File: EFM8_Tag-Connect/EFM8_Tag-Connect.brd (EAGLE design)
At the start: 10 parts, among them J1 MF-CON-2.54mm-01x08, J2 MF-CON-2.54mm-01x07, U1 EFM8BB10F2G-A-QFN20

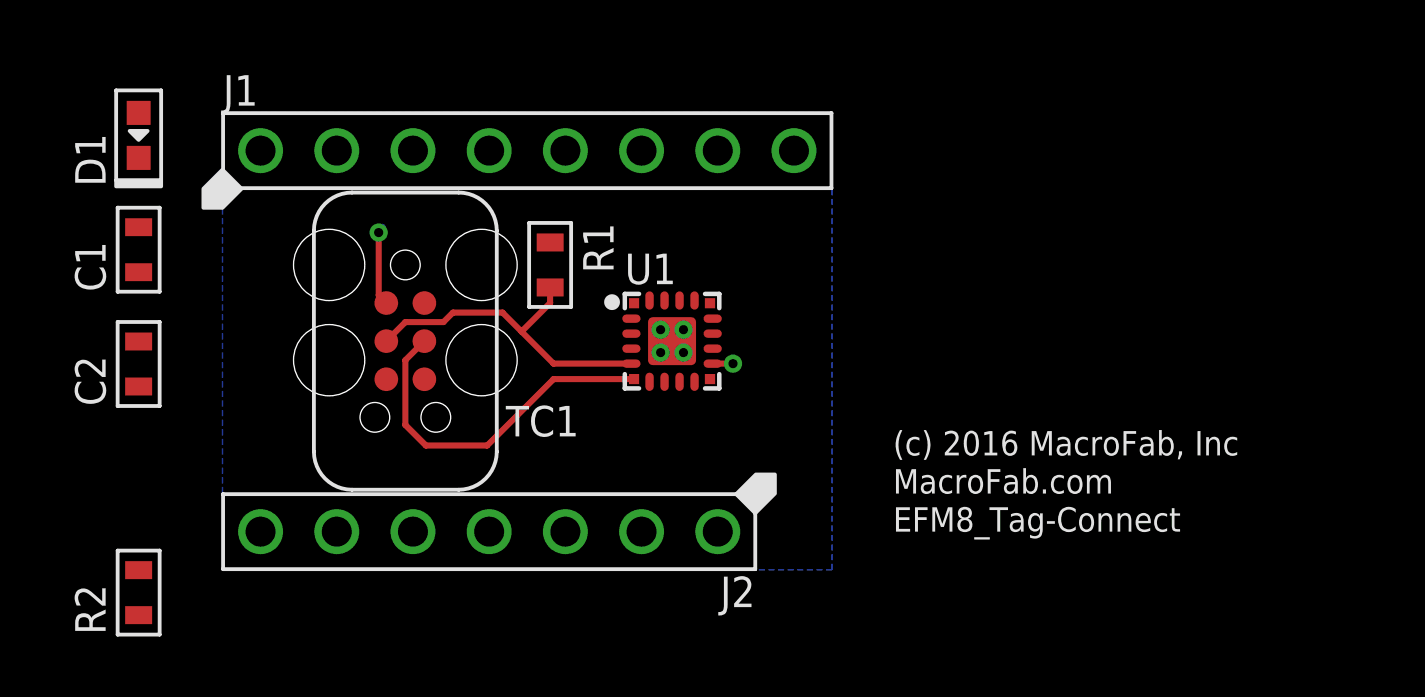
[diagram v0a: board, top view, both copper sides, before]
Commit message: Finished EFM8 board.
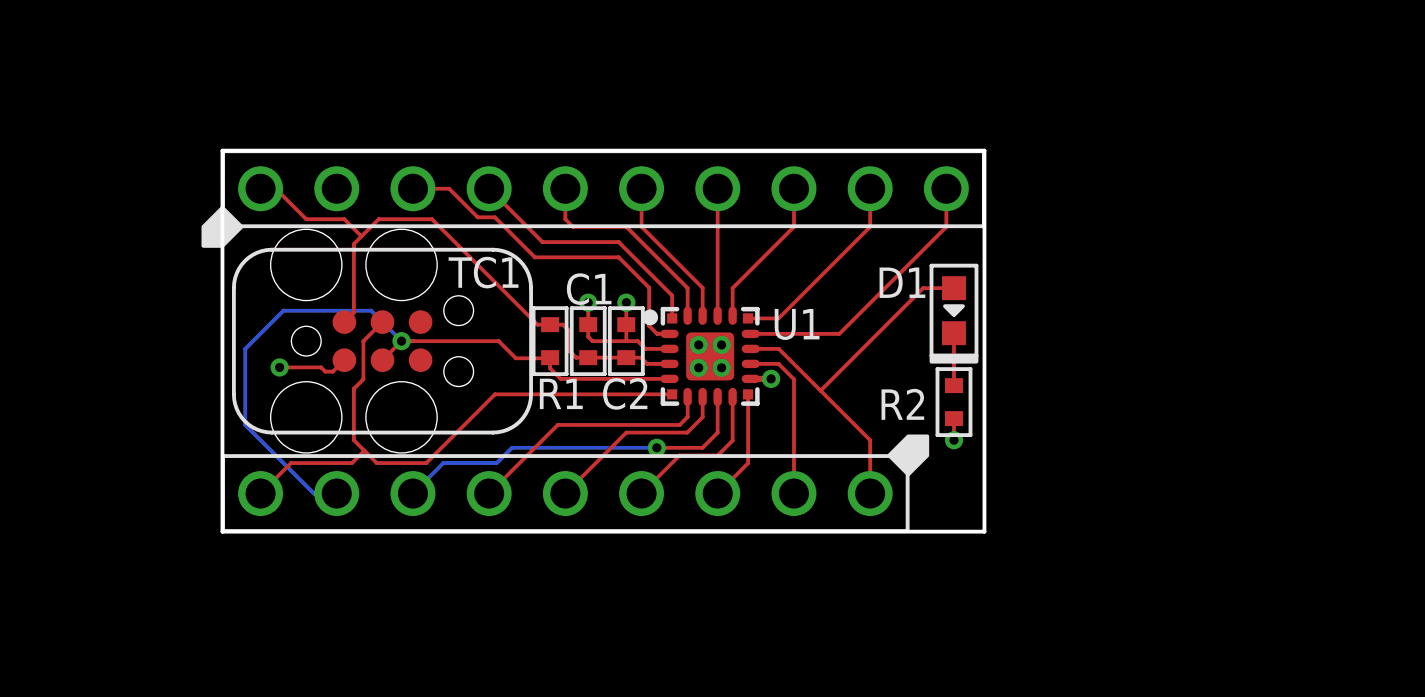
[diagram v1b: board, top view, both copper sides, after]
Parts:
- C1, C2: device MF_Passives:C0603 -> MF_Passives:C0402
- J1: value MF-CON-2.54mm-01x08 -> MF-CON-2.54mm-01x10; device MF_Connectors:PTH_2.54MM_01X08 -> MF_Connectors:PTH_2.54MM_01X10
- J2: value MF-CON-2.54mm-01x07 -> MF-CON-2.54mm-01x09; device MF_Connectors:PTH_2.54MM_01X07 -> MF_Connectors:PTH_2.54MM_01X09
- R1, R2: device MF_Passives:R0603 -> MF_Passives:R0402
- moved R2 27.9 mm to (24.4, 4.32), turned to 270 degrees
- moved D1 27.8 mm to (24.4, 7.37)
- moved C2 16.3 mm to (13.5, 6.35)
- moved C1 15.3 mm to (12.2, 6.35)
- moved FRAME1 6.51 mm to (24.6, 9.91), flipped to the bottom
- moved J1 2.84 mm to (12.7, 11.4)
- moved J2 2.84 mm to (11.4, 1.27)
- moved R1 2.54 mm to (10.9, 6.35)
- moved U1 1.37 mm to (16.3, 5.84)
- moved TC1 0.76 mm to (5.33, 6.35), turned to 0 degrees
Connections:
- net !RST!/C2CK: now also J2.P$8
- net 3.3V: now also J1.P$1
- net C2D: now also J2.P$9
- net GND: now also J1.P$2
- net P0.0: now also J1.P$3; no longer D1.ANODE, J1.P$1
- net P0.1: now also J1.P$4; no longer J1.P$2
- net P0.2: now also J1.P$5; no longer J1.P$3
- net P0.3: now also J1.P$6; no longer J1.P$4
- net P0.4: now also J1.P$7; no longer J1.P$5
- net P0.5: now also J1.P$8; no longer J1.P$6
- net P0.6: now also J1.P$9; no longer J1.P$7
- net P0.7: now also J1.P$10; no longer J1.P$8
- net P1.0: now also D1.ANODE
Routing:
- net 3.3V: track 0.00 -> 20.0 mm
- net P1.0: track 0.00 -> 12.9 mm
- net !RST!/C2CK: track 11.1 -> 23.7 mm, vias 0 -> 1
- net P1.7: track 0.00 -> 12.2 mm, vias 0 -> 1
- net P0.0: track 0.00 -> 11.3 mm
- net P0.7: track 0.00 -> 9.27 mm
- net C2D: track 11.9 -> 20.3 mm
- net P1.6: track 0.00 -> 8.34 mm
- net P0.1: track 0.00 -> 8.34 mm
- net P0.2: track 0.00 -> 6.96 mm
- net P0.6: track 0.00 -> 6.60 mm
- net P1.5: track 0.00 -> 6.30 mm
- net GND: track 3.37 -> 9.61 mm, vias 6 -> 9
- net P1.1: track 0.00 -> 5.46 mm
- net P1.3: track 0.00 -> 5.22 mm
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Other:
- board outline added: 25.4 x 12.7 mm

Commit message: Updated to recent library changes.
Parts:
- U1: value EFM8BB10F2G-A-QFN20 -> (none)
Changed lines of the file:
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@@
 <?xml version="1.0" encoding="utf-8"?>
 <!DOCTYPE eagle SYSTEM "eagle.dtd">
-<eagle version="7.6.0">
+<eagle version="7.4.0">
 <drawing>
 <settings>
@@
 <attribute name="NAME" x="8.763" y="8.636" size="1.016" layer="25" font="vector" ratio="16" rot="R180" align="center"/>
 </element>
-<element name="U1" library="MF_IC_Digital" package="EFM8BB10F(2/4/8)G-A-QFN20" value="EFM8BB10F2G-A-QFN20" x="16.256" y="5.842" smashed="yes">
+<element name="U1" library="MF_IC_Digital" package="EFM8BB10F(2/4/8)G-A-QFN20" value="" x="16.256" y="5.842" smashed="yes">
 <attribute name="HOUSEPART" value="NO" x="16.256" y="5.842" size="1.778" layer="27" display="off"/>
 <attribute name="MPN" value="EFM8BB10F2G-A-QFN20" x="16.256" y="5.842" size="1.778" layer="27" display="off"/>

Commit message: Added Pin sharing support for TagConnect.
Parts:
- U1: value (none) -> EFM8BB10F2G-A-QFN20
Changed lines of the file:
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@@
 <attribute name="NAME" x="8.763" y="8.636" size="1.016" layer="25" font="vector" ratio="16" rot="R180" align="center"/>
 </element>
-<element name="U1" library="MF_IC_Digital" package="EFM8BB10F(2/4/8)G-A-QFN20" value="" x="16.256" y="5.842" smashed="yes">
+<element name="U1" library="MF_IC_Digital" package="EFM8BB10F(2/4/8)G-A-QFN20" value="EFM8BB10F2G-A-QFN20" x="16.256" y="5.842" smashed="yes">
 <attribute name="HOUSEPART" value="NO" x="16.256" y="5.842" size="1.778" layer="27" display="off"/>
 <attribute name="MPN" value="EFM8BB10F2G-A-QFN20" x="16.256" y="5.842" size="1.778" layer="27" display="off"/>
